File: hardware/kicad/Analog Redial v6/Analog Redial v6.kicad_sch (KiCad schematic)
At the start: 76 parts, among them J1 Barrel_Jack_PTH_Slot, J2 PINHD_1x8_Male, J3 PINHD_1x2_Male, J4 PINHD_1x2_Male, J5 PINHD_2x4_Male, J6 PINHD_1x5_Male, J7 PINHD_1x3_Male, J8 RJ12, J9 RJ12, U1 ESP32-C6-DevKitC-1, U2 ES8388, U3 AG1171, U4 AG1171, U5 XC6206P362MR

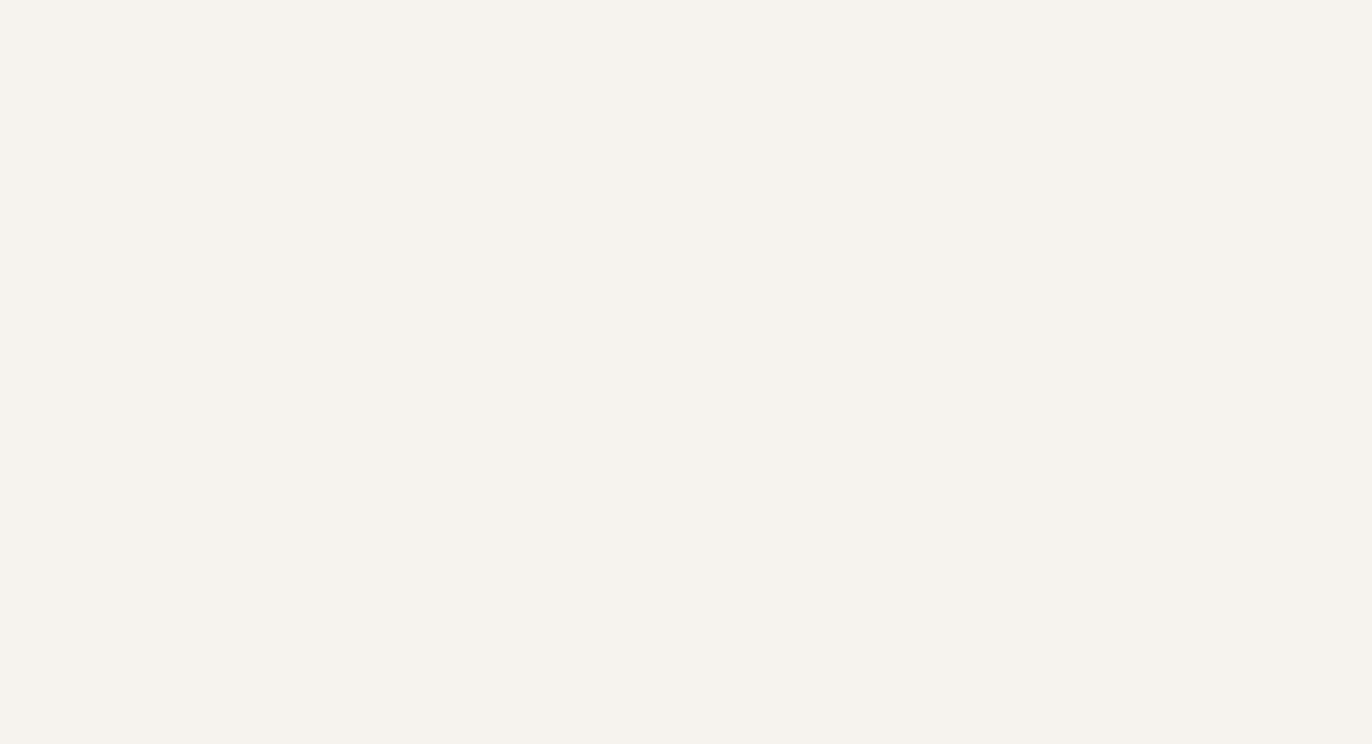
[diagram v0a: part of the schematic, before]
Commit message: v6 schematic: TCA9534APWR I2C expander (U6, 0x38, TSSOP-16, C206010) drives line 2's SLIC so line 2 and microSD work together (J5 left open); R18/R19 10k pulldowns on F/R and RM, C27 decoupling, J10 brings out spare P4-P7. Not on the PCB yet
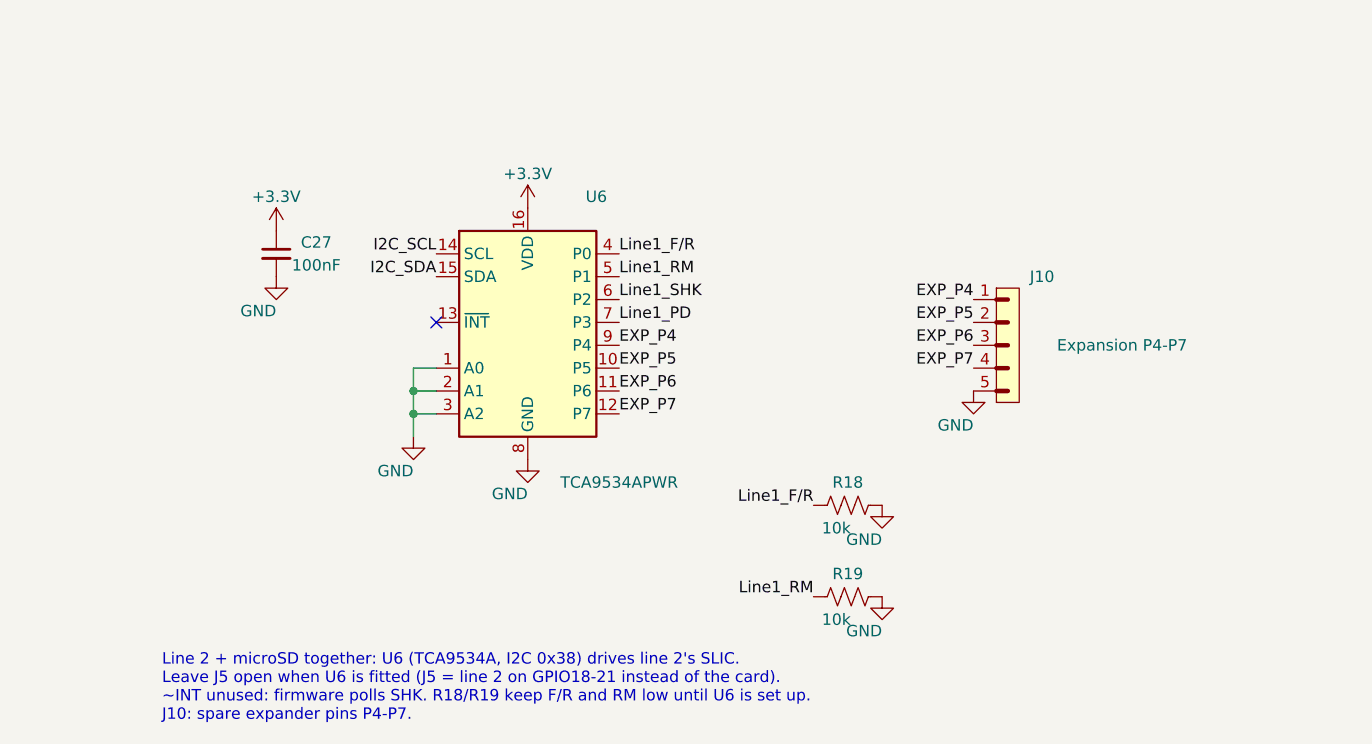
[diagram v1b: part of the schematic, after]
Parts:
- added C27: 100nF, Capacitor_SMD:C_0402_1005Metric, symbol PCM_SparkFun-Capacitor:C_Small
- added J10: Expansion P4-P7, Connector_PinHeader_2.54mm:PinHeader_1x05_P2.54mm_Vertical, symbol PCM_SL_Pin_Headers:PINHD_1x5_Male
- added R18, R19: 10k, Resistor_SMD:R_0402_1005Metric, symbol PCM_SparkFun-Resistor:R
- added U6: TCA9534APWR, Package_SO:TSSOP-16_4.4x5mm_P0.65mm, symbol Interface_Expansion:TCA9534
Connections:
- net +3.3V: now also C27.1, U6.16 (VDD)
- net GND: now also C27.2, J10.5, R18.1, R19.1, U6.1 (A0), U6.2 (A1), U6.3 (A2), U6.8 (GND)
- net I2C_SCL: now also U6.14 (SCL)
- net I2C_SDA: now also U6.15 (SDA)
- net Line1_F/R: now also R18.2, U6.4 (P0)
- net Line1_PD: now also U6.7 (P3)
- net Line1_RM: now also R19.2, U6.5 (P1)
- net Line1_SHK: now also U6.6 (P2)
- new net EXP_P4: J10.1, U6.9 (P4)
- new net EXP_P5: J10.2, U6.10 (P5)
- new net EXP_P6: J10.3, U6.11 (P6)
- new net EXP_P7: J10.4, U6.12 (P7)
- no-connect marks 0 -> 1
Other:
- note added: "Line 2 + microSD together: U6 (TCA9534A, I2C 0x38) drives line 2's SLIC. Leave J5 open when U6 is fitted (J5 = line 2 on GPIO18-21 instead of the card). ~INT unused: firmware polls SHK. R18/R19 keep F/R and RM low until U6 is set up. J10: spare expander pins P4-P7."
